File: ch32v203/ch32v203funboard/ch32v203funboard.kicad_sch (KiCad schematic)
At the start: 21 parts, among them J1 HDR, J3 PGM, J4 USB_C_Receptacle_USB2.0, J5 HDR, SW1 BOOT, U2 SRV05-4, U3 XC6206P332, Y2 8MHz

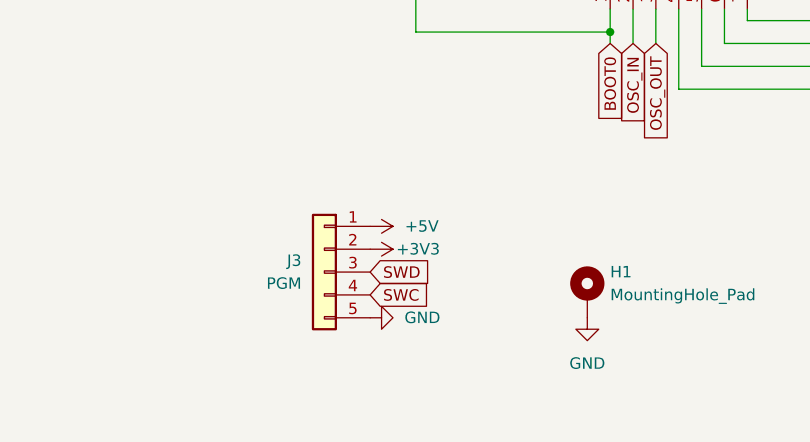
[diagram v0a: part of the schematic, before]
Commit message: Tweak pinout
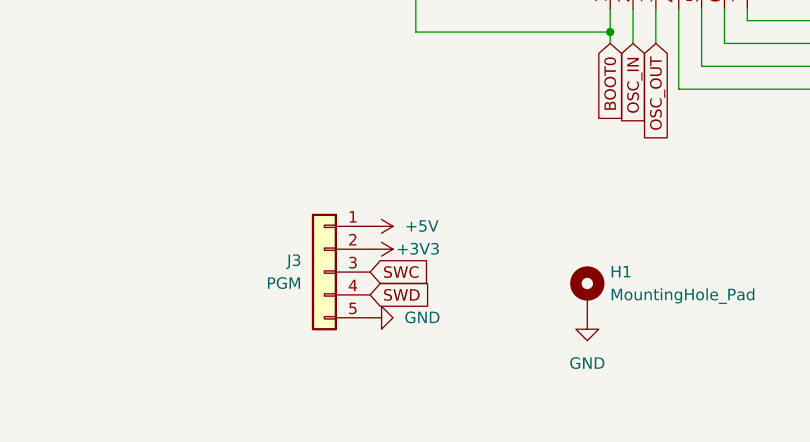
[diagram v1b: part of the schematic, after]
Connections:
- net SWC: now also J3.3 (Pin_3); no longer J3.4 (Pin_4)
- net SWD: now also J3.4 (Pin_4); no longer J3.3 (Pin_3)
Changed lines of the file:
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@@
 	(global_label "SWC"
+		(shape input)
+		(at 96.52 128.27 0)
+		(fields_autoplaced yes)
+		(effects
+			(font
+				(size 1.27 1.27)
+			)
+			(justify left)
+		)
+		(property "Intersheetrefs" "${INTERSHEET_REFS}"
+			(at 103.4361 128.27 0)
+			(effects
+				(font
+					(size 1.27 1.27)
+				)
+				(justify left)
+				(hide yes)
+			)
+		)
+	)
+	(global_label "SWD"
 		(shape input)
 		(at 96.52 130.81 0)
@@
 			(effects
 				(font
-					(size 1.27 1.27)
-				)
-				(justify left)
-				(hide yes)
-			)
-		)
-	)
-	(global_label "SWD"
-		(shape input)
-		(at 96.52 128.27 0)
-		(fields_autoplaced yes)
-		(effects
-			(font
-				(size 1.27 1.27)
-			)
-			(justify left)
-		)
-		(property "Intersheetrefs" "${INTERSHEET_REFS}"
-			(at 103.4361 128.27 0)
-			(effects
-				(font

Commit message: Bump board
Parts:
- removed J1, J5: HDR, Connector_PinHeader_2.54mm:PinHeader_2x12_P2.54mm_Vertical, symbol Connector_Generic:Conn_02x12_Odd_Even
- added J1, J2: HEADER, Connector_PinHeader_2.54mm:PinHeader_2x13_P2.54mm_Vertical, symbol Connector_Generic:Conn_02x13_Odd_Even
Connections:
- net +3V3: now also J1.21 (Pin_21), J1.22 (Pin_22), J2.5 (Pin_5), J2.6 (Pin_6)
- net +5V: now also J2.1 (Pin_1), J2.2 (Pin_2)
- net BOOT0: now also J2.25 (Pin_25), J2.26 (Pin_26)
- net D+: now also J2.11 (Pin_11), J2.12 (Pin_12)
- net D-: now also J2.10 (Pin_10), J2.9 (Pin_9)
- net GND: now also J1.25 (Pin_25), J1.26 (Pin_26), J2.3 (Pin_3), J2.4 (Pin_4)
- net NRST: now also J1.23 (Pin_23), J1.24 (Pin_24)
- net PA0: now also J1.19 (Pin_19), J1.20 (Pin_20)
- net PA1: now also J1.17 (Pin_17), J1.18 (Pin_18)
- net PA15: now also J2.13 (Pin_13), J2.14 (Pin_14)
- net PA2: now also J1.15 (Pin_15), J1.16 (Pin_16)
- net PA3: now also J1.13 (Pin_13), J1.14 (Pin_14)
- net PA4: now also J1.11 (Pin_11), J1.12 (Pin_12)
- net PA5: now also J1.10 (Pin_10), J1.9 (Pin_9)
- net PA6: now also J1.7 (Pin_7), J1.8 (Pin_8)
- net PA7: now also J1.5 (Pin_5), J1.6 (Pin_6)
- net PA9: now also J2.7 (Pin_7), J2.8 (Pin_8)
- net PB0: now also J1.3 (Pin_3), J1.4 (Pin_4)
- net PB1: now also J1.1 (Pin_1), J1.2 (Pin_2)
- net PB3: now also J2.15 (Pin_15), J2.16 (Pin_16)
- net PB4: now also J2.17 (Pin_17), J2.18 (Pin_18)
- net PB5: now also J2.19 (Pin_19), J2.20 (Pin_20)
- net PB6: now also J2.21 (Pin_21), J2.22 (Pin_22)
- net PB7: now also J2.23 (Pin_23), J2.24 (Pin_24)

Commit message: Bump designs
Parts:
- J3: LCSC (none) -> C492404
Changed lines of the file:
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@@
 			)
 		)
-		(property "LCSC" ""
+		(property "LCSC" "C492404"
 			(at 91.44 128.27 0)
 			(effects
